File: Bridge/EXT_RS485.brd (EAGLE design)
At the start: 22.5 x 72 mm, 8 parts, among them IC1 SN65HVD72D, X1 V1, X2 GND, X3 V2

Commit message: Minor Changes
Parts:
- added R1, R3: 10k, RCL:0603
- added R2: 120R, RCL:0603
- added X4, X5: TERM, Conn:T1.6/0.9
- moved C1 1.65 mm to (3.81, 14.1)
- moved IC1 1.65 mm to (8.00, 16.6)
- moved X1 1.65 mm to (16.4, 30.9), turned to 180 degrees
- moved X2 1.65 mm to (16.4, 28.3), turned to 180 degrees
- moved X3 1.65 mm to (16.4, 25.8), turned to 180 degrees
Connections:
- new net N$13: R2.1, X4.1
- net +3V3: now also R3.2
- net DE: now also R1.2
- net GND: now also R1.1
- net N$11: now also R2.2
- net N$12: now also X5.1
- net RX: now also R3.1
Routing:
- net N$12: track 5.56 -> 12.4 mm
- net N$11: track 6.08 -> 11.8 mm
- net VIN: track 79.2 -> 82.4 mm
- net N$13: track 0.00 -> 1.86 mm
- net +3V3: track 54.9 -> 56.7 mm
- net RX: track 55.4 -> 56.8 mm
- net TX: track 54.5 -> 55.8 mm
- net DE: track 68.0 -> 69.3 mm

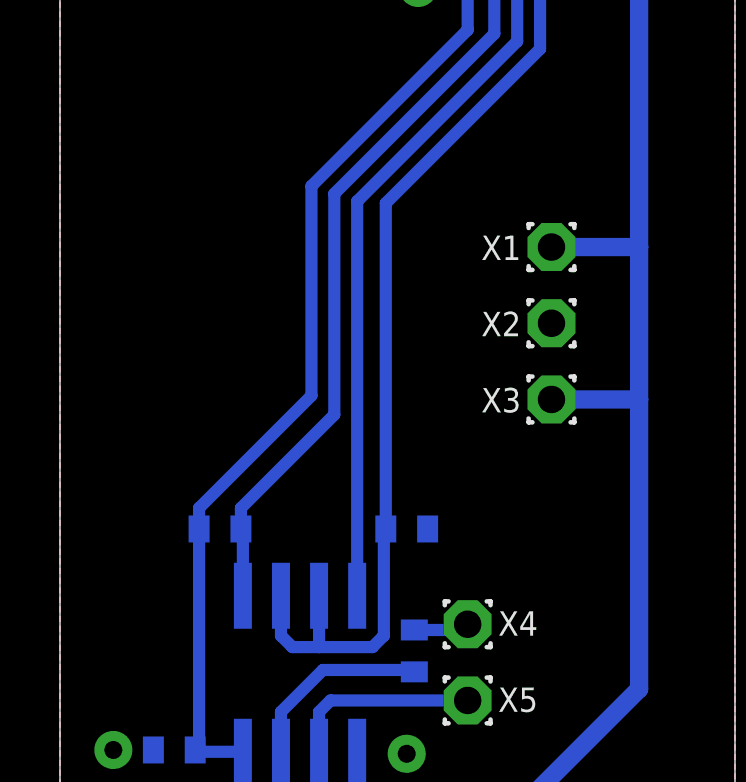
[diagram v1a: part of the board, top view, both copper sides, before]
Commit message: Added LED's
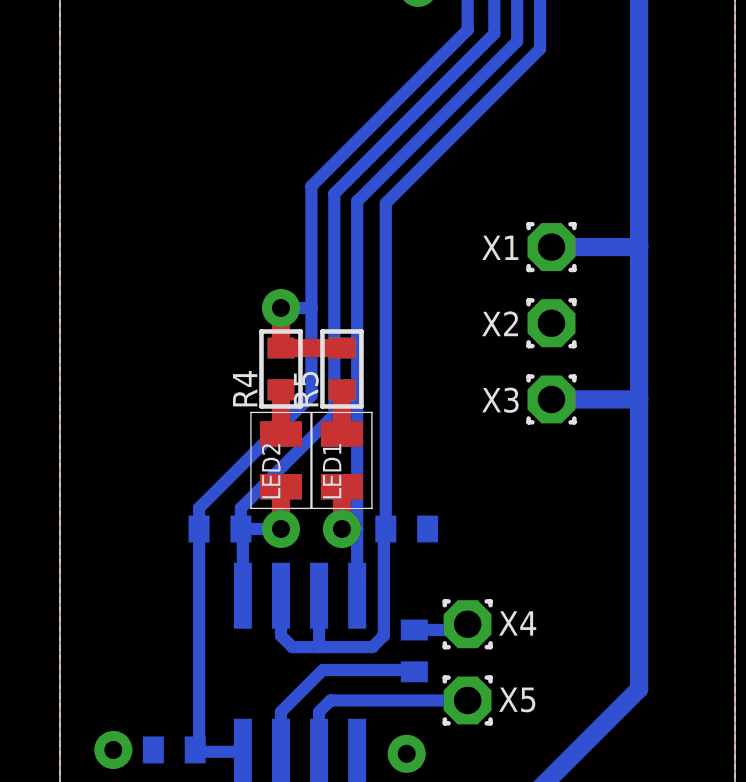
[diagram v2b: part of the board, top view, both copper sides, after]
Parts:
- added LED1, LED2: (no value), Optic:0805
- added R4, R5: 10k, RCL:0603
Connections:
- new net N$14: LED2.C, R4.1
- new net N$15: LED1.C, R5.1
- net +3V3: now also R4.2, R5.2
- net RX: now also LED2.A
- net TX: now also LED1.A
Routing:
- net +3V3: track 56.7 -> 61.0 mm, vias 0 -> 1
- net RX: track 56.8 -> 59.6 mm, vias 0 -> 1
- net TX: track 55.8 -> 57.7 mm, vias 0 -> 1
- net N$15: track 0.00 -> 1.47 mm
- net N$14: track 0.00 -> 1.47 mm
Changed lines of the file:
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@@
 <setting verticaltext="up"/>
 </settings>
-<grid distance="5" unitdist="mil" unit="mil" style="lines" multiple="1" display="no" altdistance="0.025" altunitdist="inch" altunit="inch"/>
+<grid distance="5" unitdist="mil" unit="mm" style="lines" multiple="1" display="no" altdistance="0.025" altunitdist="inch" altunit="inch"/>
 <layers>
 <layer number="1" name="Top" color="4" fill="1" visible="yes" active="yes"/>
@@
 <rectangle x1="6.477" y1="12.7" x2="6.985" y2="12.827" layer="42"/>
 <rectangle x1="13.335" y1="16.637" x2="13.843" y2="17.399" layer="42"/>
+<rectangle x1="6.477" y1="23.495" x2="10.287" y2="24.003" layer="41"/>
 </plain>
 <attributes>
@@
 <element name="X5" library="Conn" package="T1.6/0.9" value="TERM" x="13.589" y="15.748"/>
 <element name="R3" library="RCL" package="0603" value="10k" x="5.334" y="21.463" rot="MR0"/>
+<element name="LED1" library="Optic" package="0805" value="" x="9.398" y="23.749" rot="R270"/>
+<element name="LED2" library="Optic" package="0805" value="" x="7.366" y="23.749" rot="R270"/>
+<element name="R4" library="RCL" package="0603" value="10k" x="7.366" y="26.797" rot="R90"/>
+<element name="R5" library="RCL" package="0603" value="10k" x="9.398" y="26.797" rot="R90"/>
 </elements>
 <signals>
@@
 <wire x1="9.144" y1="25.273" x2="9.144" y2="32.639" width="0.4064" layer="16"/>
 <wire x1="9.144" y1="32.639" x2="14.478" y2="37.973" width="0.4064" layer="16"/>
+<contactref element="LED2" pad="A"/>
+<wire x1="6.0314" y1="21.463" x2="7.366" y2="21.463" width="0.4064" layer="16"/>
+<via x="7.366" y="21.463" extent="1-16" drill="0.6" diameter="1.27"/>
+<wire x1="7.366" y1="21.463" x2="7.366" y2="22.8692" width="0.6096" layer="1"/>
 </signal>
 <signal name="TX">
@@
 <wire x1="11.43" y1="64.389" x2="15.24" y2="60.579" width="0.4064" layer="16"/>
 <wire x1="15.24" y1="60.579" x2="15.24" y2="37.719" width="0.4064" layer="16"/>
-<wire x1="9.906" y1="19.237" x2="9.906" y2="32.385" width="0.4064" layer="16"/>
+<wire x1="9.906" y1="19.237" x2="9.906" y2="21.463" width="0.4064" layer="16"/>
+<wire x1="9.906" y1="21.463" x2="9.906" y2="32.385" width="0.4064" layer="16"/>
 <wire x1="9.906" y1="32.385" x2="15.24" y2="37.719" width="0.4064" layer="16"/>
+<contactref element="LED1" pad="A"/>
+<wire x1="9.398" y1="22.8692" x2="9.398" y2="21.463" width="0.6096" layer="1"/>
+<via x="9.398" y="21.463" extent="1-16" drill="0.6" diameter="1.27"/>
+<wire x1="9.398" y1="21.463" x2="9.906" y2="21.463" width="0.4064" layer="16"/>
 </signal>
 <signal name="DE">
@@
 <wire x1="4.6366" y1="21.463" x2="4.6366" y2="22.1626" width="0.4064" layer="16"/>
 <wire x1="4.6366" y1="22.1626" x2="8.382" y2="25.908" width="0.4064" layer="16"/>
-<wire x1="8.382" y1="25.908" x2="8.382" y2="32.893" width="0.4064" layer="16"/>
+<wire x1="8.382" y1="25.908" x2="8.382" y2="28.829" width="0.4064" layer="16"/>
+<wire x1="8.382" y1="28.829" x2="8.382" y2="32.893" width="0.4064" layer="16"/>
 <wire x1="8.382" y1="32.893" x2="13.589" y2="38.1" width="0.4064" layer="16"/>
+<contactref element="R4" pad="2"/>
+<contactref element="R5" pad="2"/>
+<wire x1="7.366" y1="27.4944" x2="7.366" y2="28.829" width="0.6096" layer="1"/>
+<via x="7.366" y="28.829" extent="1-16" drill="0.6" diameter="1.27"/>
+<wire x1="7.366" y1="28.829" x2="8.382" y2="28.829" width="0.4064" layer="16"/>
+<wire x1="9.398" y1="27.4944" x2="7.366" y2="27.4944" width="0.6096" layer="1"/>
 </signal>
 <signal name="N$11">
@@
 <wire x1="13.3974" y1="18.0964" x2="13.589" y2="18.288" width="0.4064" layer="16"/>
 </signal>
+<signal name="N$14">
+<contactref element="LED2" pad="C"/>
+<contactref element="R4" pad="1"/>
+<wire x1="7.366" y1="24.6288" x2="7.366" y2="26.0996" width="0.6096" layer="1"/>
+</signal>
+<signal name="N$15">
+<contactref element="LED1" pad="C"/>
+<contactref element="R5" pad="1"/>
+<wire x1="9.398" y1="24.6288" x2="9.398" y2="26.0996" width="0.6096" layer="1"/>
+</signal>
 </signals>

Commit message: Added S4M13
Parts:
- removed BUS: BUS, Conn:1725672
- removed LED1, LED2: (no value), Optic:0805
- removed R4, R5: 10k, RCL:0603
- removed X1: V1, Conn:T1.6/0.9
- removed X2: GND, Conn:T1.6/0.9
- removed X3: V2, Conn:T1.6/0.9
- added C2: nc, RCL:1206
- added CN1, CN2: RJ11, Conn:69254
- added D1: PMEG4005, Diode:SOD323
- added IC2: TSR 0.5-2450, DCDC:SIP3
- moved R1 40.5 mm to (16.9, 61.6)
- moved R3 37.4 mm to (13.7, 57.9)
- moved IC1 36.2 mm to (15.9, 51.9)
- moved C1 34.1 mm to (14.0, 46.6), turned to 90 degrees
- moved X4 15.4 mm to (2.54, 7.49)
- moved X5 15.4 mm to (2.54, 4.95)
- moved R2 14.0 mm to (8.00, 3.94), turned to 180 degrees
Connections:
- net N$13 renamed BUS-R
- removed net N$12: BUS.2, IC1.6, X5.1
- removed net N$14: LED2.C, R4.1
- removed net N$15: LED1.C, R5.1
- new net BUS-A: CN1.-3, CN2.-3, IC1.6, X5.1
- new net BUS-B: CN1.-2, CN2.-2, IC1.7, R2.2
- new net VOUT: IC2.P$3, IN.P$1
- net +3V3: no longer R4.2, R5.2
- net GND: now also C2.1, CN1.-5, CN2.-5, IC2.P$2; no longer BUS.4, X2.1
- net N$11: now also C2.2, D1.C, IC2.P$1; no longer BUS.1, IC1.7, R2.2
- net RX: no longer LED2.A
- net TX: no longer LED1.A
- net VIN: now also CN1.-4, CN2.-4, D1.A; no longer BUS.3, IN.P$1, X1.1, X3.1
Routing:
- net BUS-A: track 0.00 -> 59.0 mm
- net BUS-B: track 0.00 -> 49.6 mm
- net VOUT: track 0.00 -> 45.3 mm, vias 0 -> 1
- net +3V3: track 61.0 -> 19.5 mm, vias 1 -> 0
- net RX: track 59.6 -> 18.2 mm, vias 1 -> 0
- net TX: track 57.7 -> 19.4 mm, vias 1 -> 0
- net DE: track 69.3 -> 33.3 mm
- net N$12: track 12.4 -> 0.00 mm
- net N$11: track 11.8 -> 5.64 mm
- net VIN: track 82.4 -> 86.8 mm, vias 0 -> 3
- net BUS-R: track 1.86 -> 6.24 mm
- net N$15: track 1.47 -> 0.00 mm
- net N$14: track 1.47 -> 0.00 mm
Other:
- board text removed: "+"
- board text removed: "-"
- board text removed: "A"
- board text removed: "B"
